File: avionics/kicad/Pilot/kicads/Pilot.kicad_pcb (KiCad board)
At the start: 6 copper layers, 55 x 35 mm, 120 parts, among them X2Y-CAN 4.7nF X2Y, X2Y-RS485 4.7nF X2Y

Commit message: Pilot: grid router (scripts/grid_route_pilot.py); 123 -> 119 unconnected, DRC 0
Rule-aware A* router used in place of freerouting (which hangs on boards that
already carry copper). Four routing layers (F, In2, In3, B) with through vias;
GND/+3V3 pads drop to the In1/In4 planes. Enforces 0.127 mm clearance, 0.5 mm
ISOLATION cross-domain, 0.3 mm edge with the 3 mm corner arcs, hole clearance
0.25 / hole-to-hole 0.5, ISO_BAND rules with full via/track extent, and the
In2-In4 band keep-outs (isolated nets: F.Cu only, no vias). Router copper never
relabels another net's cells. Each pass is followed by zone refill and
repair_pilot_routing.py.

Board: DRC 0 errors, parity 0, 119 unconnected. The remainder is walled in by
existing copper (a board-wide search found no legal path), so further gains
need rip-up-and-reroute.

Co-Authored-By: Claude Opus 5.5 (1M context) <noreply@anthropic.com>
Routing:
- net ETH_RXN: track 10.2 -> 46.5 mm, vias 1 -> 4
- net PGND: track 211.8 -> 219.6 mm, vias 4 -> 5
- net +5V: track 138.3 -> 140.1 mm, vias 7 -> 8
- net GND: track 244.1 -> 245.4 mm, vias 23 -> 24

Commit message: Pilot: rip-up-and-reroute pass (119 -> 118 unconnected, DRC 0)
grid_route_pilot.py --ripup: a connection with no legal path may cross other
nets' PRE-EXISTING tracks/vias (never pads, holes, edge or band rules) at
0.25 mm per cell; the items its new copper would violate are measured
(segment/segment and via distances incl. 0.5 mm cross-domain and hole-to-hole),
ripped (max 8 per route) and their nets rerouted by the following normal
passes. Best board kept by unconnected count with DRC 0 errors, parity 0.

Co-Authored-By: Claude Opus 5.5 (1M context) <noreply@anthropic.com>
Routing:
- net MDIO0: track 40.6 -> 0.45 mm, vias 3 -> 0
- net +5V: track 140.1 -> 102.2 mm, vias 8 -> 12
- net IMU_INT2: track 0.00 -> 37.5 mm, vias 0 -> 3
- net RS485_DE: track 39.7 -> 4.23 mm, vias 3 -> 0
- net RMII0_REF_CLK: track 35.7 -> 0.44 mm, vias 2 -> 0
- net SPI0_CLK: track 32.7 -> 1.21 mm, vias 3 -> 1
- net M1553_IRQN: track 38.6 -> 7.18 mm, vias 2 -> 1
- net PGND: track 219.6 -> 189.0 mm, vias 5 -> 6
- net ETH_RXN: track 46.5 -> 18.4 mm, vias 4 -> 3
- net RMII0_TXD1: track 26.9 -> 0.00 mm, vias 2 -> 0
- net ETH2_BS: track 39.5 -> 17.0 mm, vias 2 -> 3
- net CAN_STB: track 22.5 -> 0.35 mm, vias 2 -> 0
- net RMII1_TXD1: track 0.00 -> 21.6 mm, vias 0 -> 2
- net IMU_INT1: track 0.00 -> 20.3 mm, vias 0 -> 2
- net RMII0_TX_EN: track 43.5 -> 23.4 mm, vias 4 -> 3
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
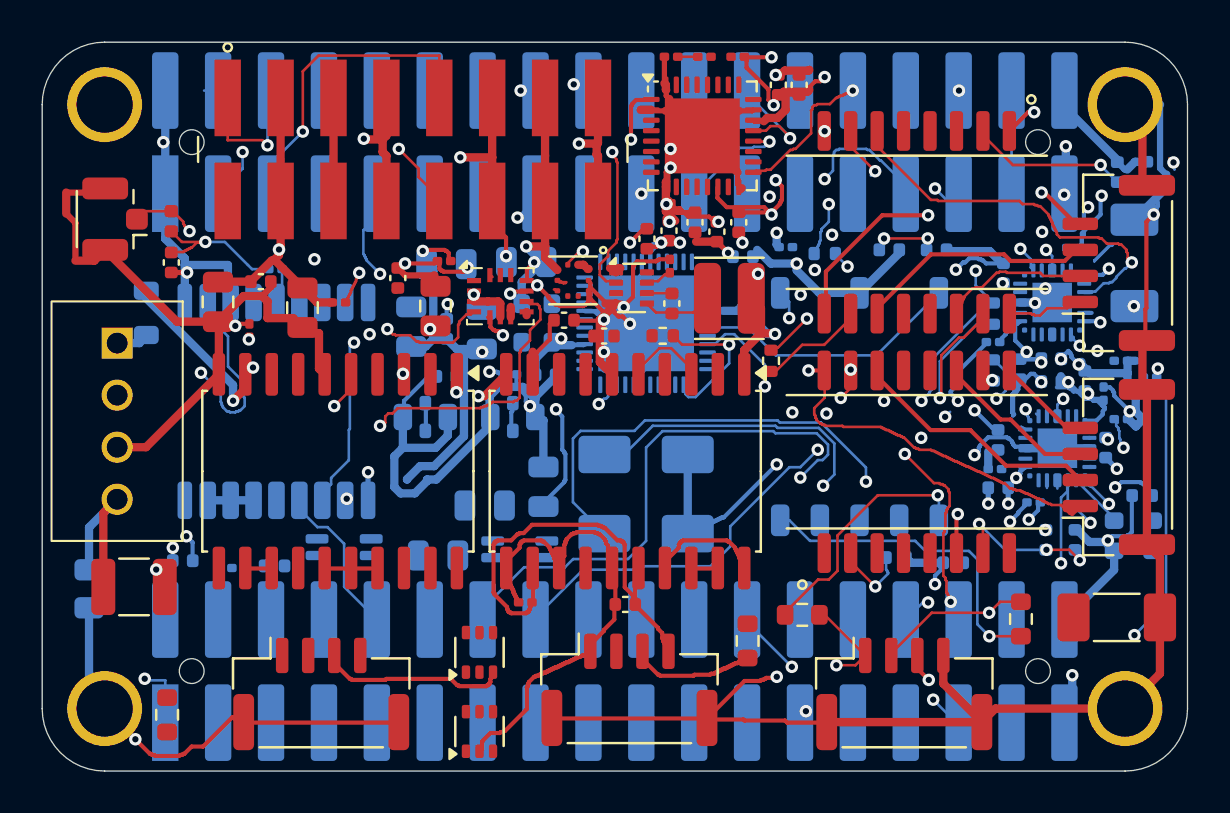
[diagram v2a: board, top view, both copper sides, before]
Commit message: Pilot: alternating route / rip-up rounds (118 -> 110 unconnected, DRC 0)
Three rounds of grid_route_pilot.py (two normal passes then a --ripup pass,
zone refill + repair after each); best board kept. Verified in the repo:
DRC 0 errors, parity 0, 110 unconnected. A fourth round gave no gain; a
clean-slate run of the same router plateaued at 131 and was discarded.

Co-Authored-By: Claude Opus 5.5 (1M context) <noreply@anthropic.com>
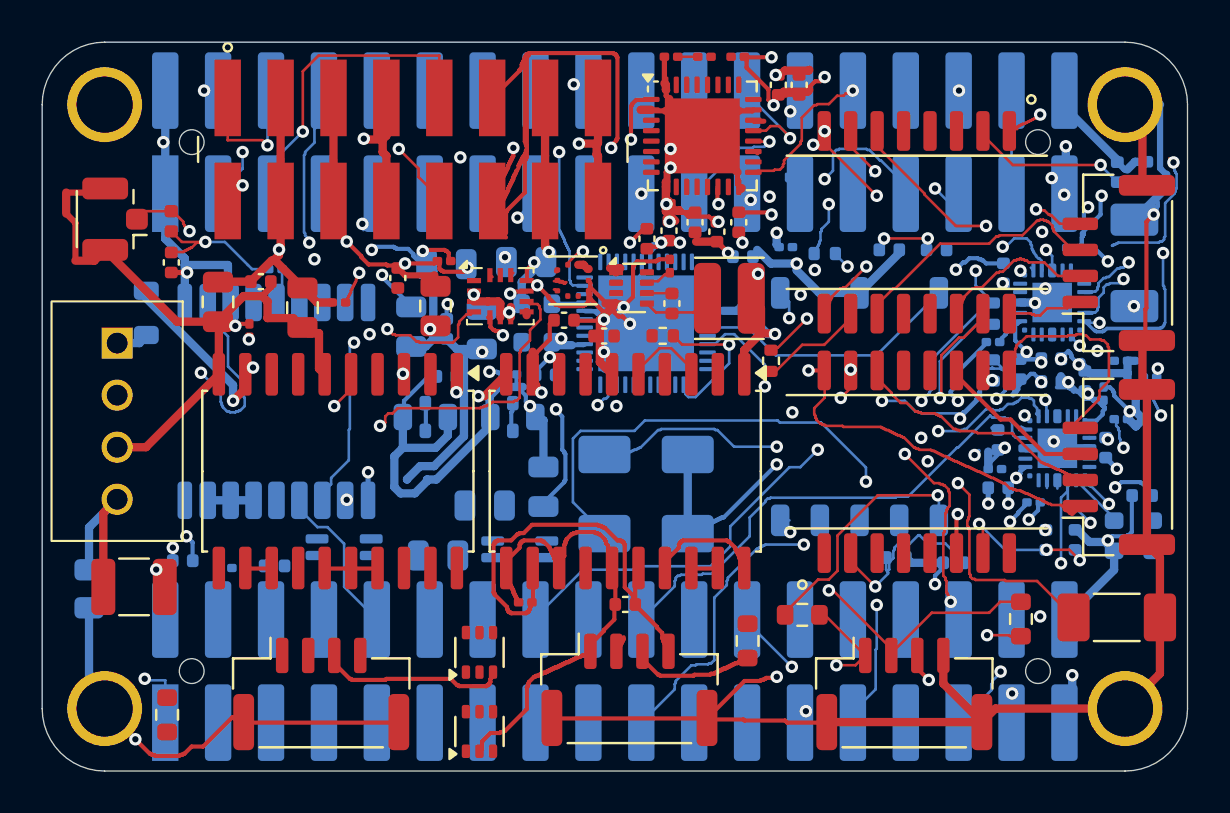
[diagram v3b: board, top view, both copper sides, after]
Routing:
- net +5V: track 102.2 -> 168.6 mm, vias 12 -> 16
- net PHY2_INTRN: track 40.9 -> 0.52 mm, vias 2 -> 0
- net RMII0_REF_CLK: track 0.44 -> 29.6 mm, vias 0 -> 2
- net M1553_MRN: track 0.00 -> 28.9 mm, vias 0 -> 2
- net RMII1_REF_CLK: track 0.00 -> 28.9 mm, vias 0 -> 3
- net RMII1_RX_ER: track 0.00 -> 24.0 mm
- net RMII0_TXD1: track 0.00 -> 23.9 mm, vias 0 -> 2
- net U3V3_EN: track 23.9 -> 2.41 mm, vias 2 -> 1
- net PHY1_RSTN: track 20.9 -> 0.57 mm, vias 4 -> 2
- net ETH2_BS: track 17.0 -> 37.2 mm, vias 3 -> 5
- net SPI0_MISO: track 0.17 -> 13.3 mm, vias 0 -> 2
- net RMII0_TX_EN: track 23.4 -> 10.4 mm, vias 3 -> 2
- net RMII0_RXD1: track 11.3 -> 0.00 mm, vias 2 -> 0
- net ETH_TXP: track 14.1 -> 24.4 mm, vias 2 -> 3
- net BUS_1553_N: track 36.5 -> 29.0 mm
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
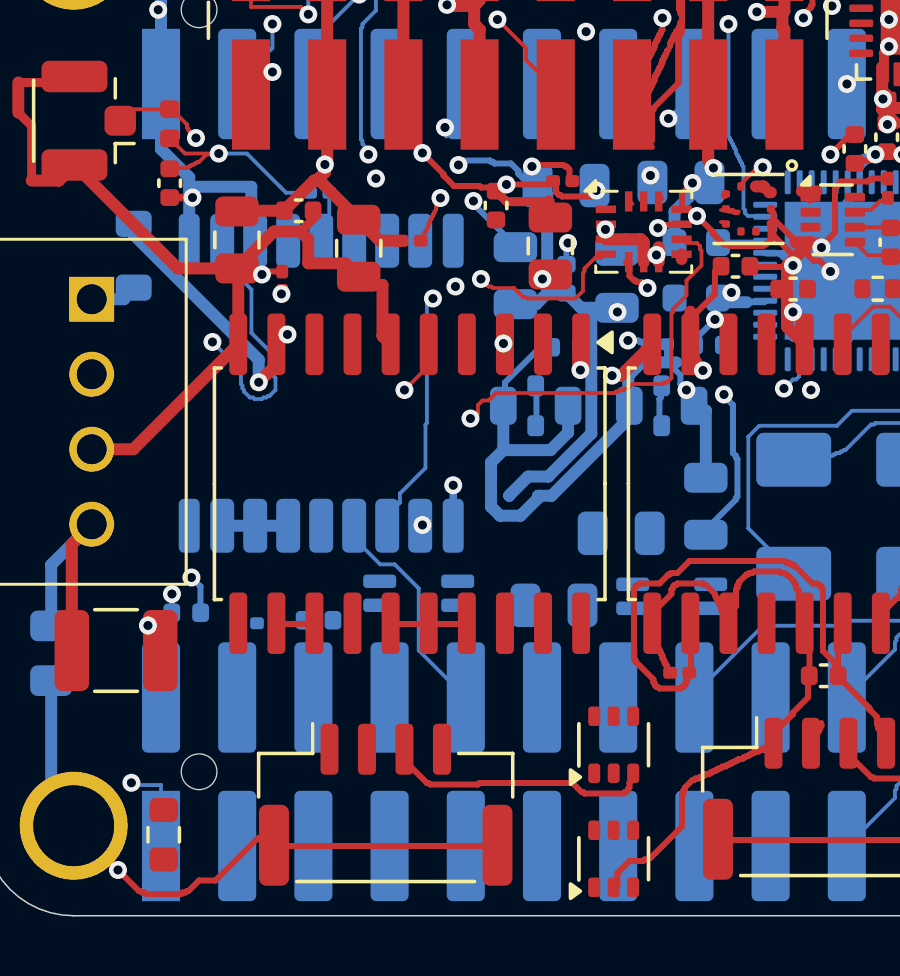
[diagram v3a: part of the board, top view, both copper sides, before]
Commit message: Pilot: C-CAN4/C-CAN6 to F.Cu inside the band (110 -> 104 unconnected, DRC 0)
Isolated-side caps on B.Cu could not connect: In2-In4 band keep-outs forbid
vias and iso_nets_stay_in_band bars iso tracks on B.Cu. The two small caps fit
the F.Cu strip between CAN-TR and the CAN-FD connector (option B, owner
choice). CMC-CAN, CMC-RS485, C-CAN5, C-485-5 have no F.Cu site yet.

Co-Authored-By: Claude Opus 5.5 (1M context) <noreply@anthropic.com>
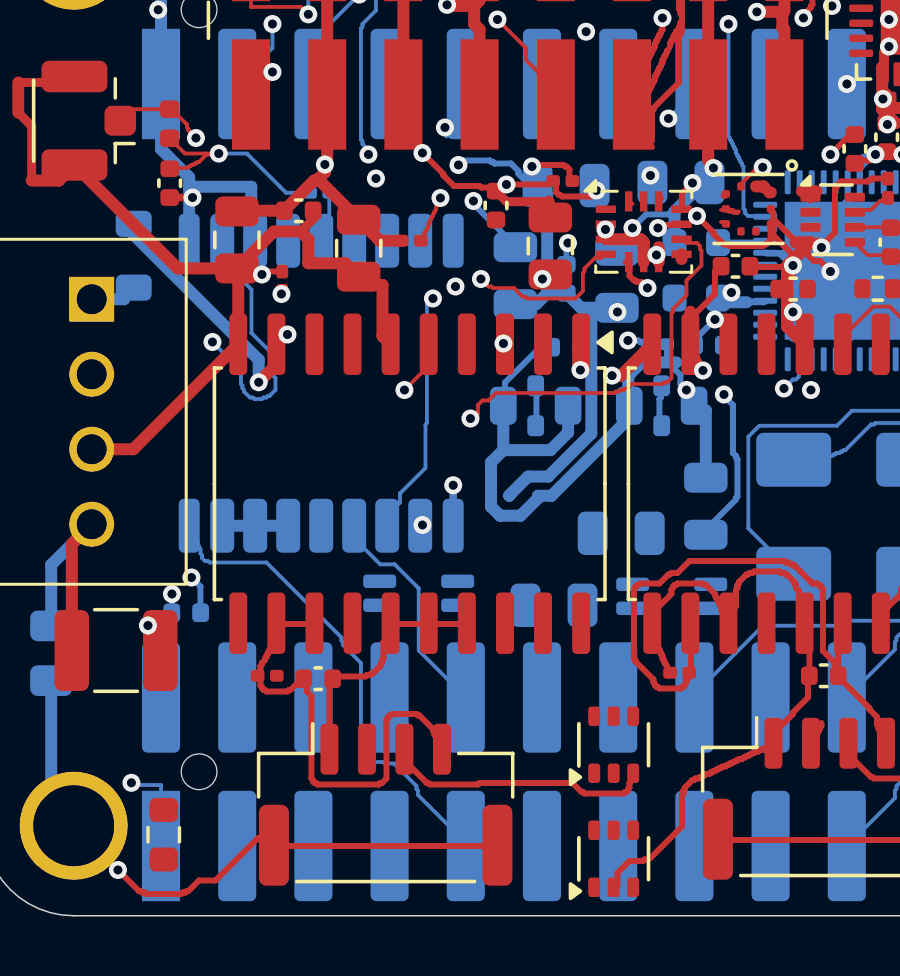
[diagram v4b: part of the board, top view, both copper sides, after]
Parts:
- C-CAN4, C-CAN6: moved to F.Cu
- moved C-CAN6 1.95 mm to (132.2, 114.6), turned to 0 degrees
- moved C-CAN4 1.75 mm to (130.4, 114.5), turned to 0 degrees
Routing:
- net GPS_RESETN: track 0.33 -> 16.4 mm
- net VCC2_CAN: track 1.25 -> 16.2 mm
- net GND2_CAN: track 3.90 -> 9.65 mm
- net GND: track 238.1 -> 241.3 mm, vias 47 -> 48
